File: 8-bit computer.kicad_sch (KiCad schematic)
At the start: 0 parts

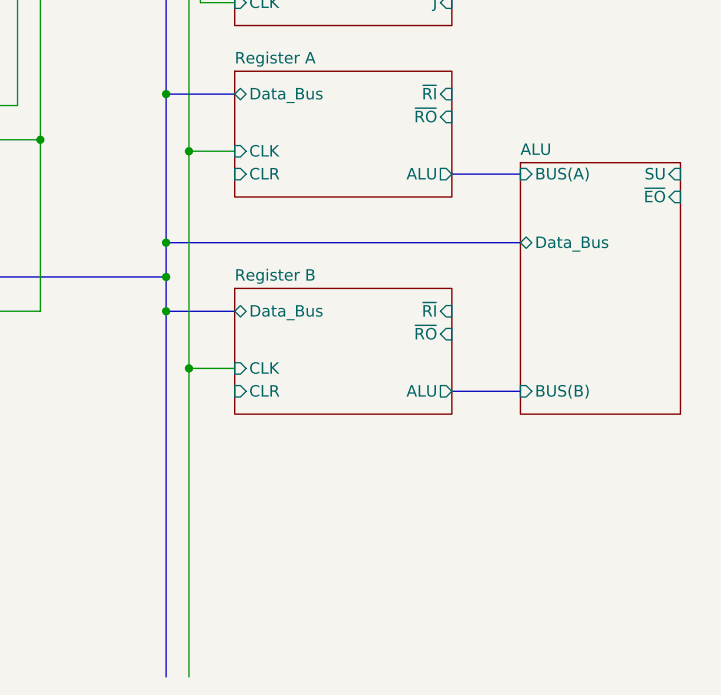
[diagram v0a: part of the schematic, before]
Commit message: Create Flag/Status Register
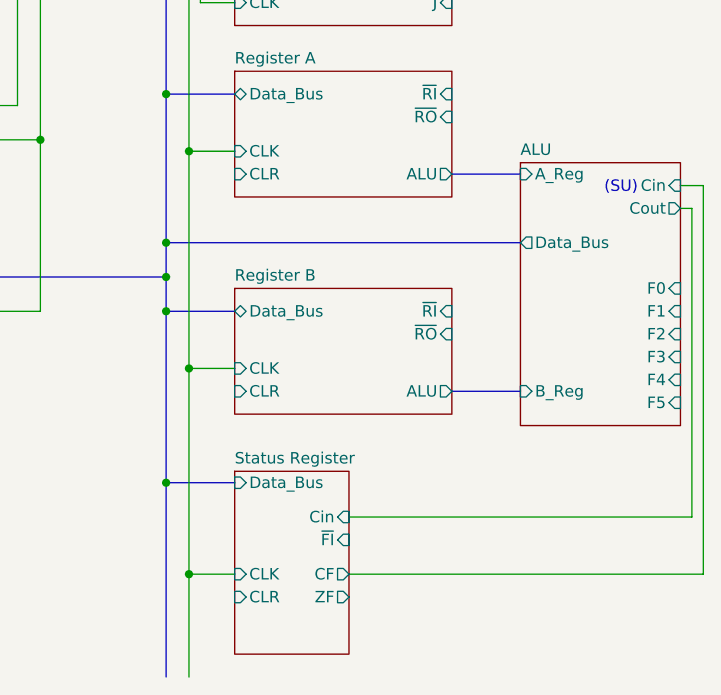
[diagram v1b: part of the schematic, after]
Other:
- added sheet Status Register (Flag Register/Flag Register.kicad_sch)
- sheet ALU: file Arithmetic logic unit/Arithmetic logic unit.kicad_sch -> ALU/ALU.kicad_sch
- sheet ALU ports: added A_Reg, B_Reg, Cin, Cout, F0, F1, F2, F3, F4, F5; removed BUS(A), BUS(B), SU, ~{EO}
- note added: "(SU)"

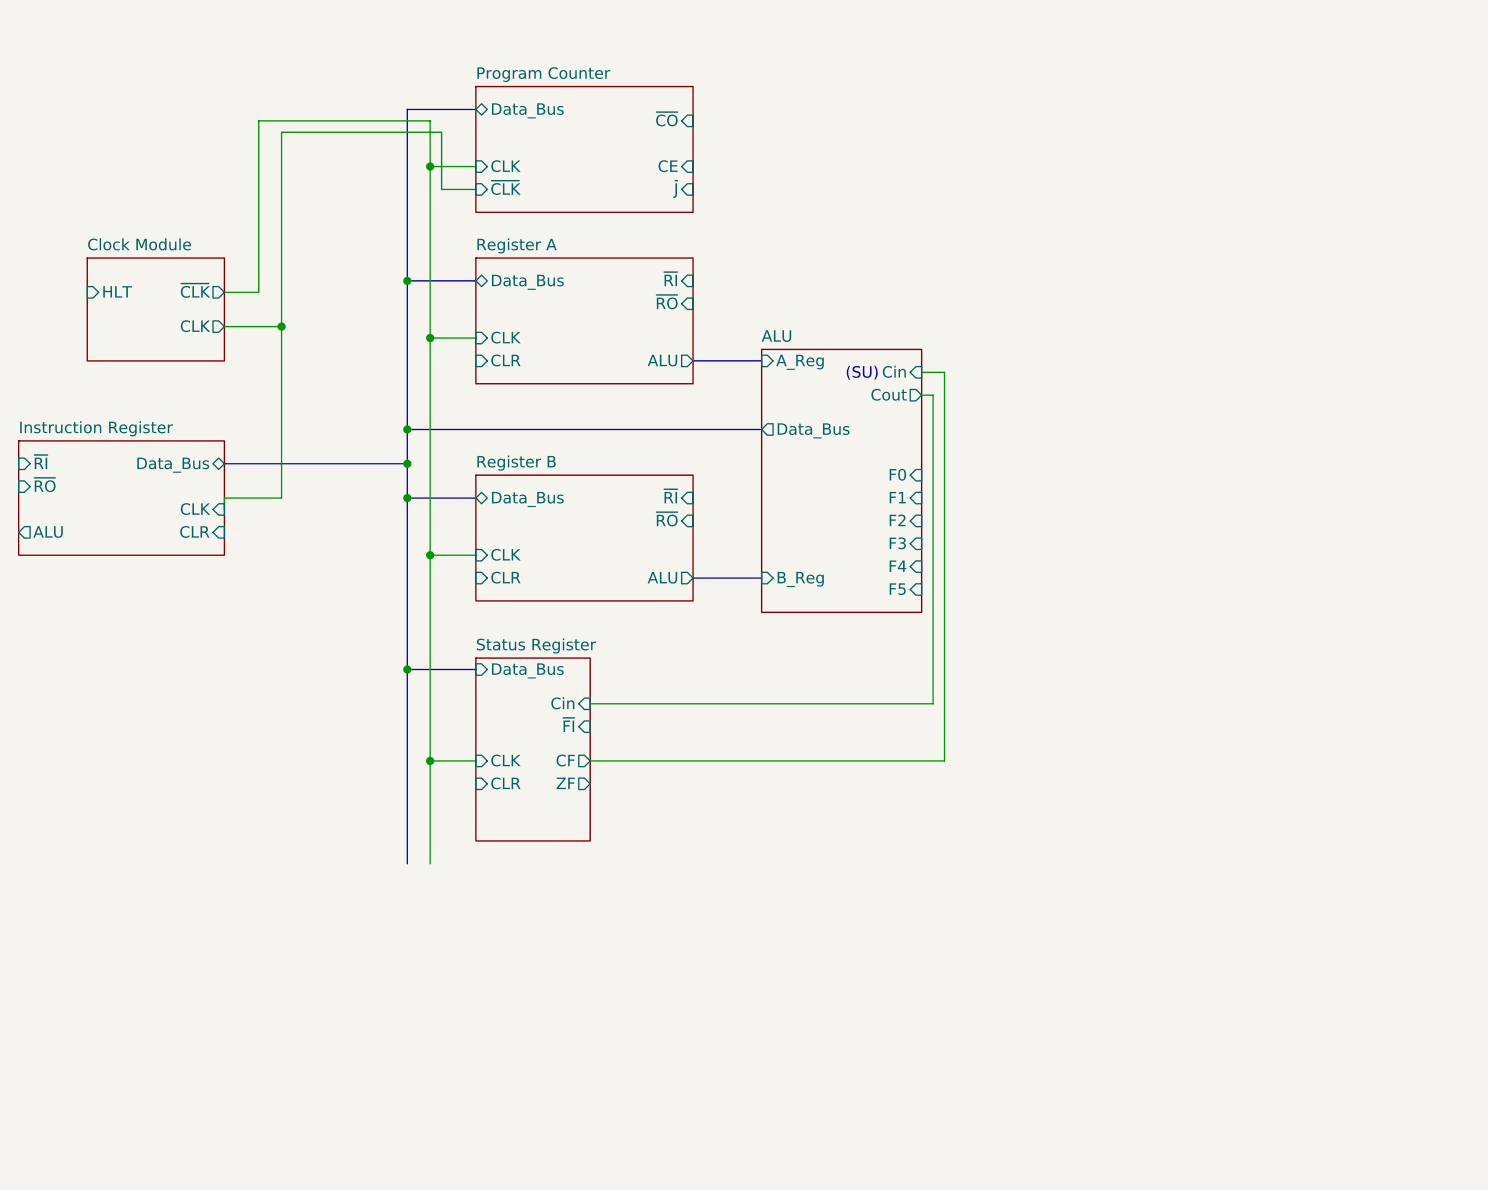
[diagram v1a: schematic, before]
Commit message: Expanding the block diagram
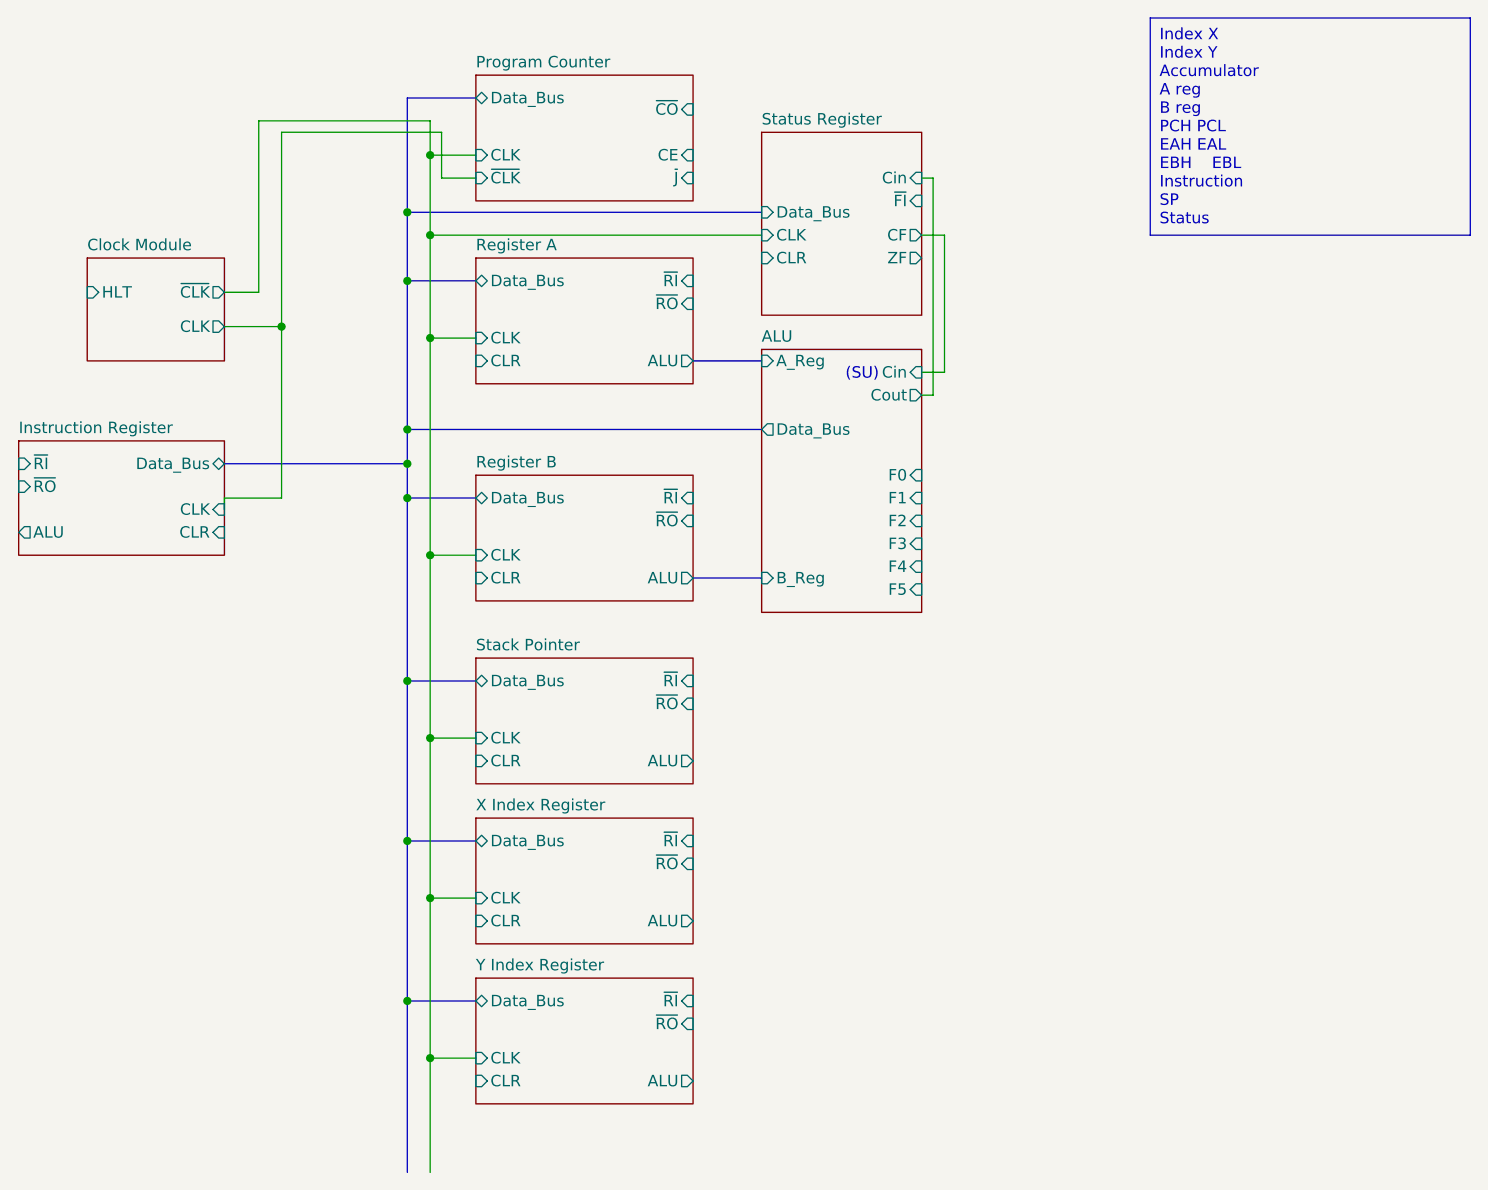
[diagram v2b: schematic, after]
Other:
- added sheet Stack Pointer (register module/register module.kicad_sch)
- added sheet X Index Register (register module/register module.kicad_sch)
- added sheet Y Index Register (register module/register module.kicad_sch)
- title: (none) -> 8-bit CMOS/TTL Computer
